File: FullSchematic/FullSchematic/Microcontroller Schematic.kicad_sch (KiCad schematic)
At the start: 19 parts, among them J1 USB_B_Micro, J3 Conn_01x24_Socket, J4 Conn_01x24_Socket, U2 CH340C, U3 24LC64

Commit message: updated schematics and footprints
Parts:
- U2: JLCPCB Part # (none) -> C84681; Price (none) -> 0.47; Price ( 1 board) (none) -> 0.47; Price (5 boards) (none) -> 2.35
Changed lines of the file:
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@@
+      (effects (font (size 1.27 1.27)) hide)
+    )
+    (property "JLCPCB Part #" "C84681" (at 191.77 62.23 0)
+      (effects (font (size 1.27 1.27)) hide)
+    )
+    (property "Price" "0.47" (at 191.77 62.23 0)
+      (effects (font (size 1.27 1.27)) hide)
+    )
+    (property "Price ( 1 board)" "0.47" (at 191.77 62.23 0)
+      (effects (font (size 1.27 1.27)) hide)
+    )
+    (property "Price (5 boards)" "2.35" (at 191.77 62.23 0)
       (effects (font (size 1.27 1.27)) hide)
     )

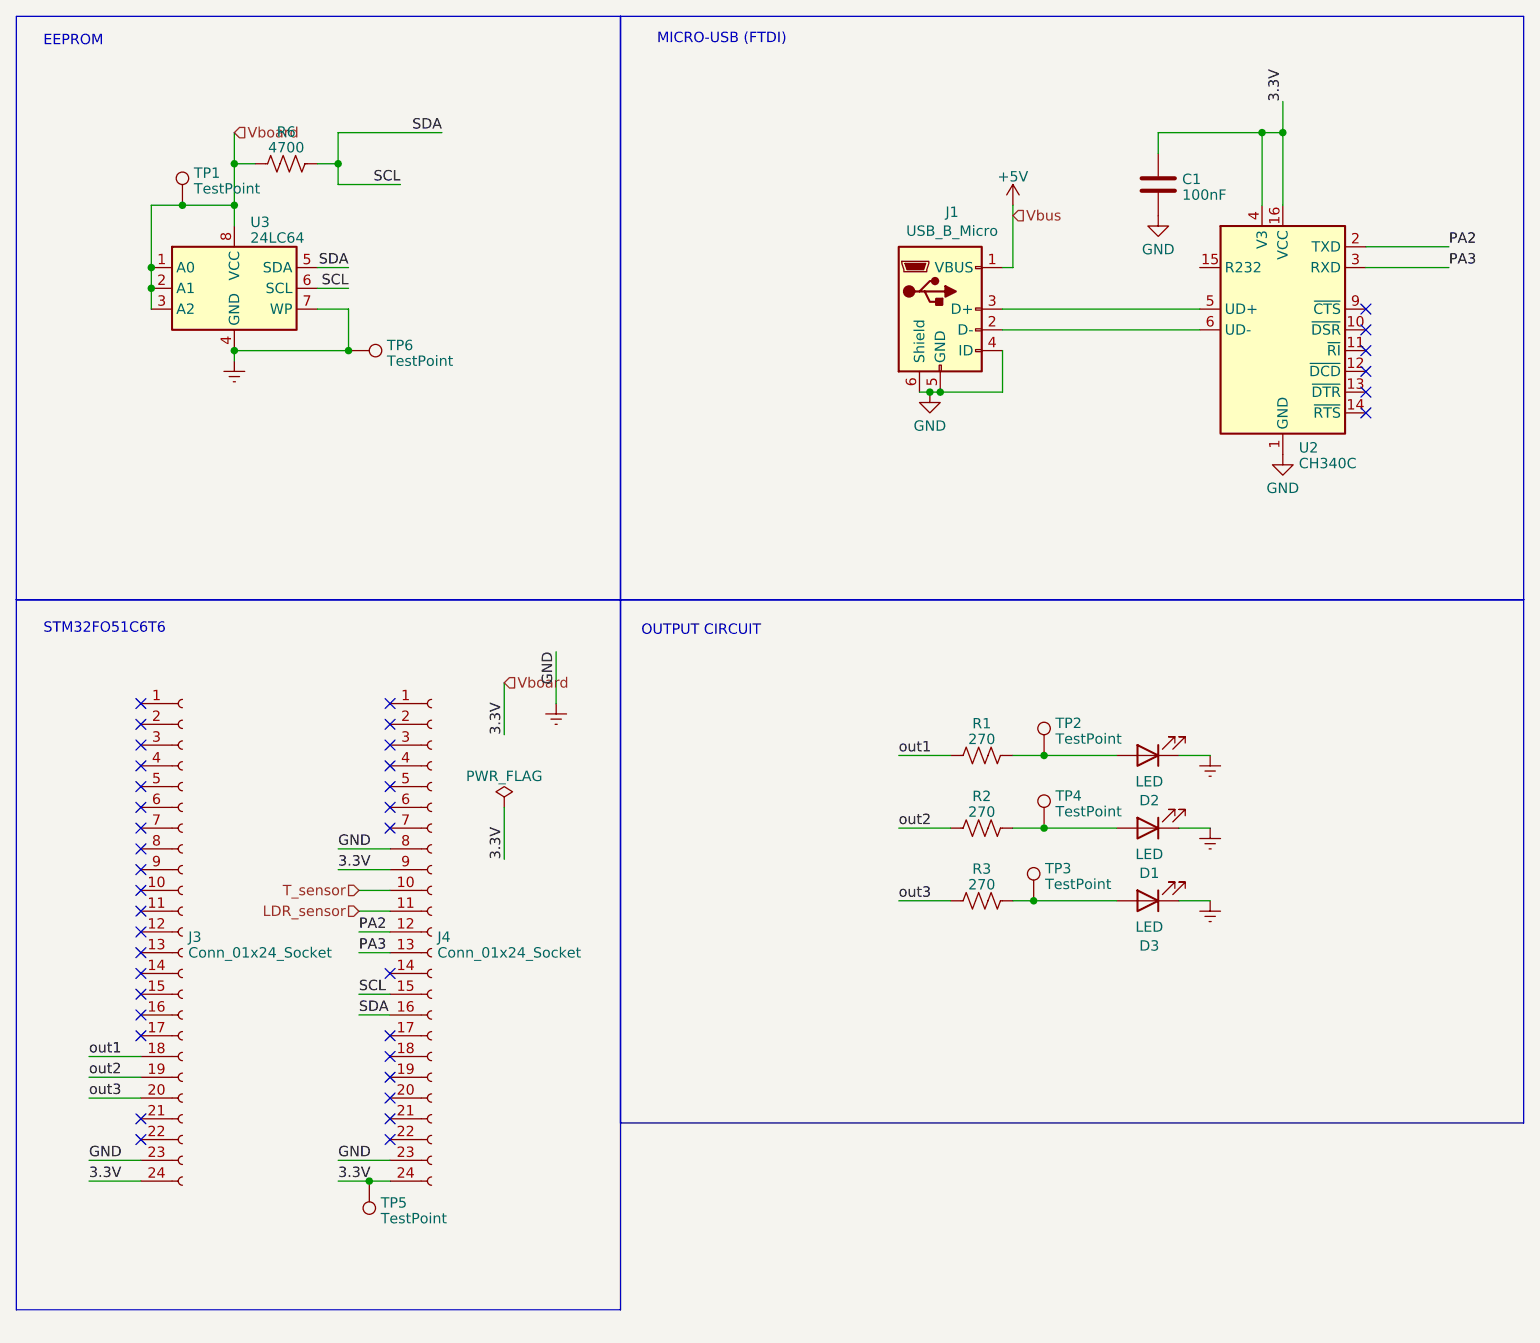
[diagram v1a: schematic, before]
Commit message: updated schematic and footprints
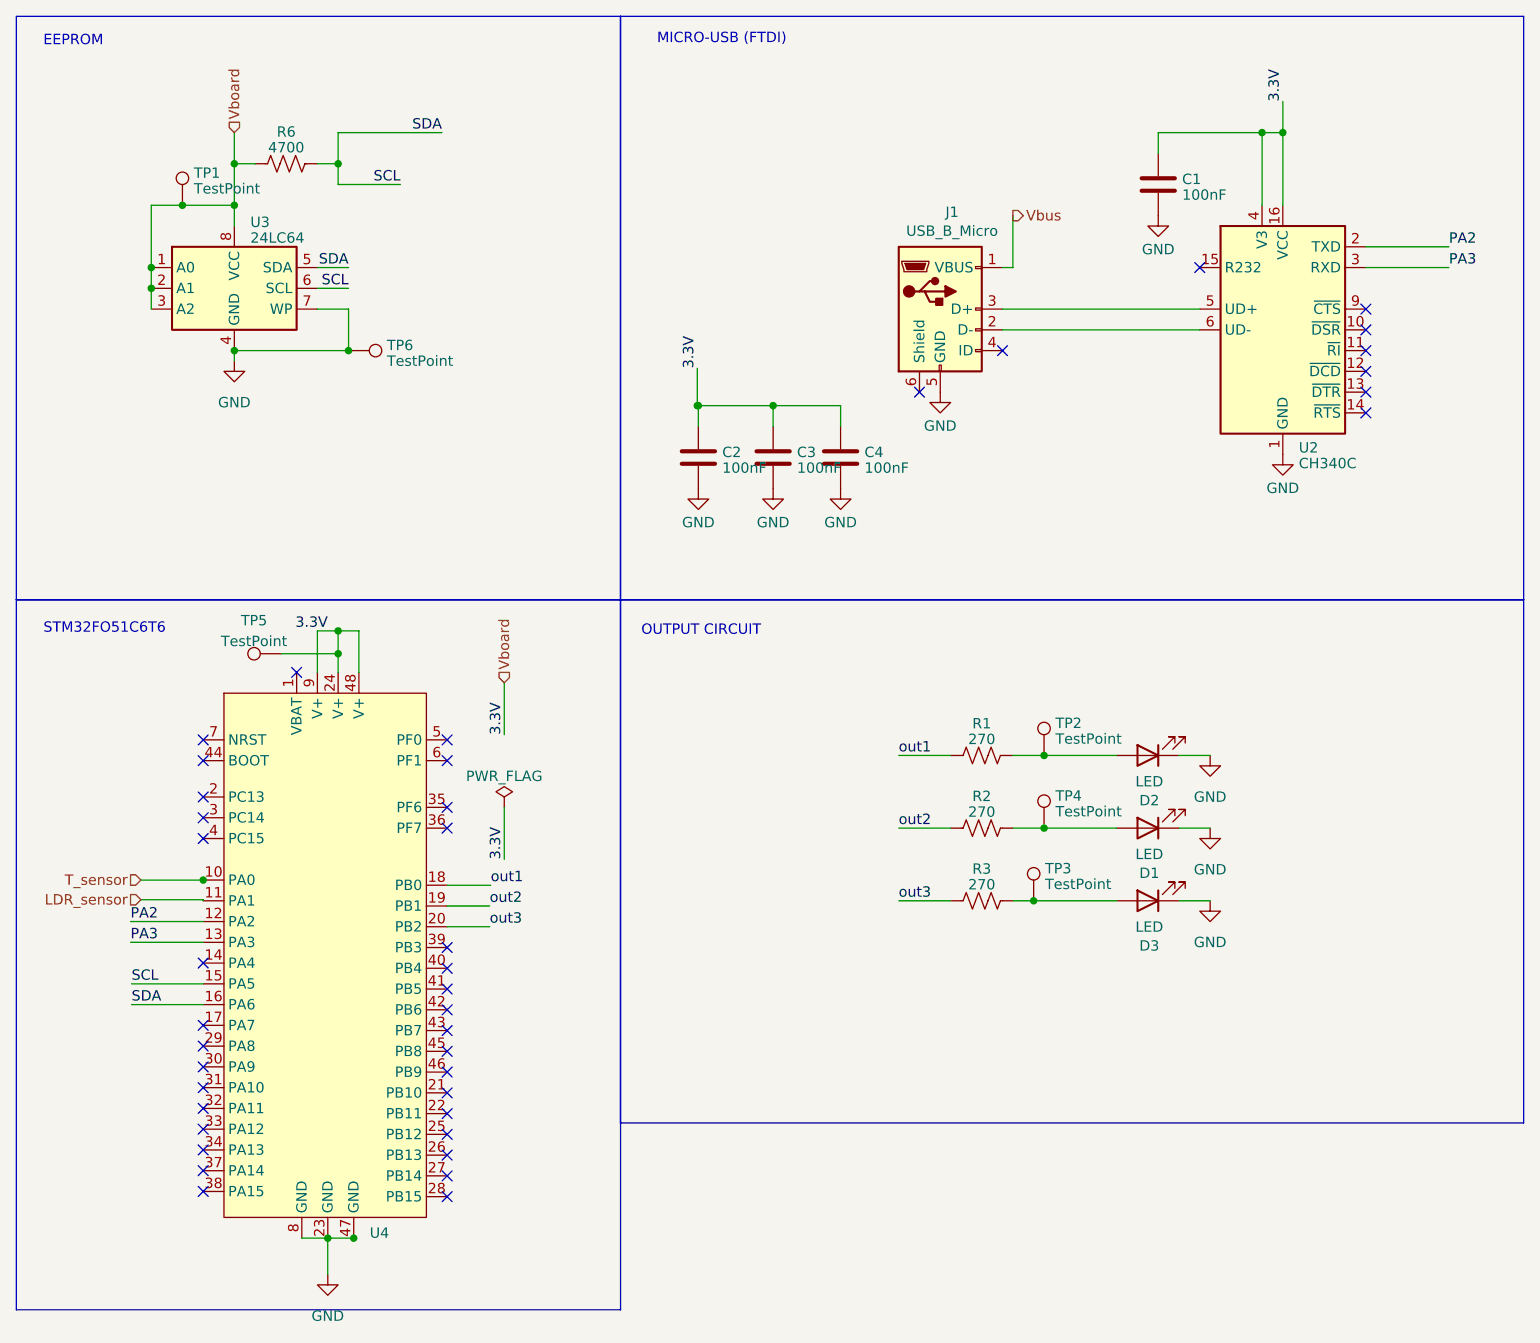
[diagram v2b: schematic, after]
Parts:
- removed J3, J4: Conn_01x24_Socket, Connector_PinSocket_1.00mm:PinSocket_1x24_P1.00mm_Vertical, symbol Connector:Conn_01x24_Socket
- added C2, C3, C4: 100nF, Library:CAPC1608X90N, symbol Device:C
- added U4: ~, Library:STM32F051C6T6, symbol UCT:STM32F051C6TG6_Target
- D1, D2, D3: footprint LED_SMD:LED-APA102-2020 -> LED_THT:LED_D3.0mm_IRBlack
- TP5: JLCPCB Part # N/A -> (none); Price $0 -> (none); Price ( 1 board) 0 -> (none); Price (5 boards) 0 -> (none)
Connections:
- net LDR_sensor: now also U4.11 (PA1)
- net PA2: now also U4.12 (PA2)
- net PA3: now also U4.13 (PA3)
- net SCL: now also U4.15 (PA5), U4.16 (PA6)
- net T_sensor: now also U4.10 (PA0)
- net Vboard: now also C2.1, C3.1, C4.1, U4.24 (V+), U4.48 (V+), U4.9 (V+)
- net out1: now also U4.18 (PB0)
- net out2: now also U4.19 (PB1)
- net out3: now also U4.20 (PB2)
- net +5V renamed Vbus
- net Earth renamed GND
- net GND: now also C2.2, C3.2, C4.2, U4.23 (GND), U4.47 (GND), U4.8 (GND); no longer J1.4 (ID), J1.6 (Shield)
- no-connect marks 39 -> 42

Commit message: connected sensors adnd created touch pad
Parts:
- TP7: renamed from TP5; JLCPCB Part # (none) -> N/A; Price (none) -> 0; Price ( 1 board) (none) -> 0; Price (5 boards) (none) -> 0
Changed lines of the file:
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@@
     (stroke (width 0) (type default))
   )
-  (wire (pts (xy 52.07 131.953) (xy 59.69 131.953))
+  (wire (pts (xy 52.07 132.08) (xy 59.69 132.08))
     (stroke (width 0) (type default))
   )
@@
   )
   (wire (pts (xy 53.34 46.99) (xy 57.15 46.99))
-    (stroke (width 0) (type default))
-  )
-  (wire (pts (xy 59.69 131.953) (xy 59.69 132.08))
     (stroke (width 0) (type default))
   )
@@
     (effects (font (size 1.27 1.27)) (justify left))
   )
-  (hierarchical_label "LDR_sensor" (shape input) (at 52.07 131.953 180) (fields_autoplaced)
+  (hierarchical_label "LDR_sensor" (shape input) (at 52.07 132.08 180) (fields_autoplaced)
     (effects (font (size 1.27 1.27)) (justify right))
   )
@@
   (symbol (lib_id "Connector:TestPoint") (at 69.215 101.854 90) (unit 1)
     (in_bom yes) (on_board yes) (dnp no) (fields_autoplaced)
-    (property "Reference" "TP5" (at 65.913 97.79 90)
+    (property "Reference" "TP7" (at 65.913 97.79 90)
       (effects (font (size 1.27 1.27)))
     )
@@
       (effects (font (size 1.27 1.27)) hide)
     )
-    (pin "1")
-    (instances
-      (project "FullSchematic"
-        (path "/5dd86611-a33d-45ee-946c-01c599f30b12/5d08bf44-0550-4275-b6e8-e4566a125a74"
-          (reference "TP5") (unit 1)
-        )
-      )
+    (property "JLCPCB Part #" "N/A" (at 69.215 101.854 0)
+      (effects (font (size 1.27 1.27)) hide)
+    )
+    (property "Price" "0" (at 69.215 101.854 0)
+      (effects (font (size 1.27 1.27)) hide)
+    )
+    (property "Price ( 1 board)" "0" (at 69.215 101.854 0)
+      (effects (font (size 1.27 1.27)) hide)
+    )
+    (property "Price (5 boards)" "0" (at 69.215 101.854 0)
+      (effects (font (size 1.27 1.27)) hide)
+    )
+    (pin "1")
+    (instances
+      (project "FullSchematic"
+        (path "/5dd86611-a33d-45ee-946c-01c599f30b12/5d08bf44-0550-4275-b6e8-e4566a125a74"
+          (reference "TP7") (unit 1)
+        )
+      )
